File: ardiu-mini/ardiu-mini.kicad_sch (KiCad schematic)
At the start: 6 parts

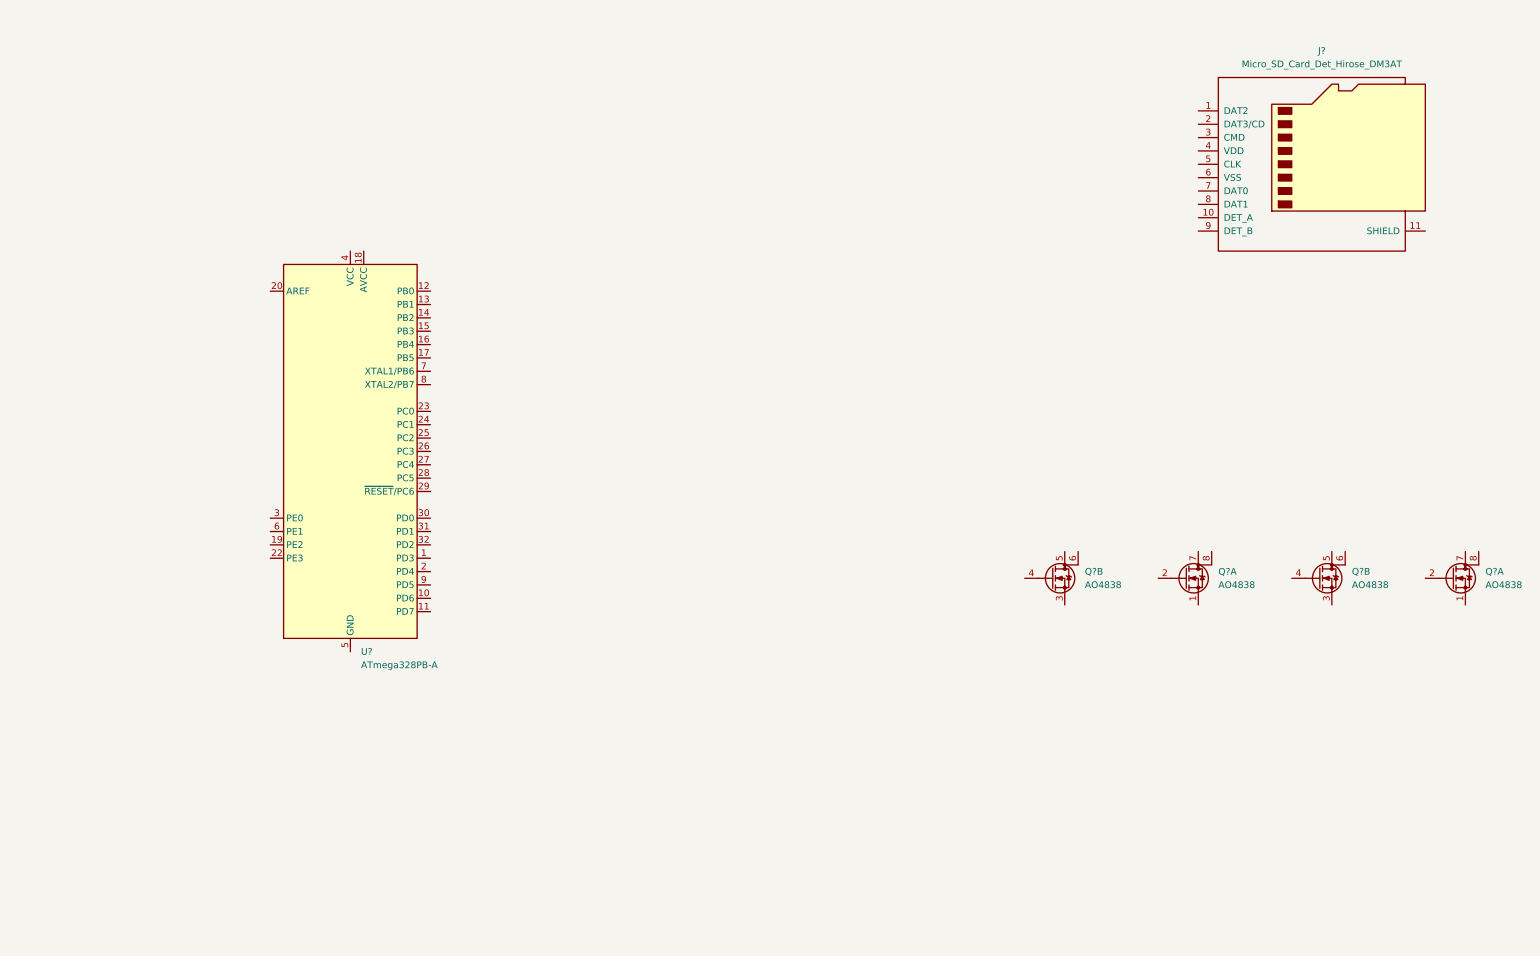
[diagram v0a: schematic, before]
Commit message: Board layout with weak grounding path
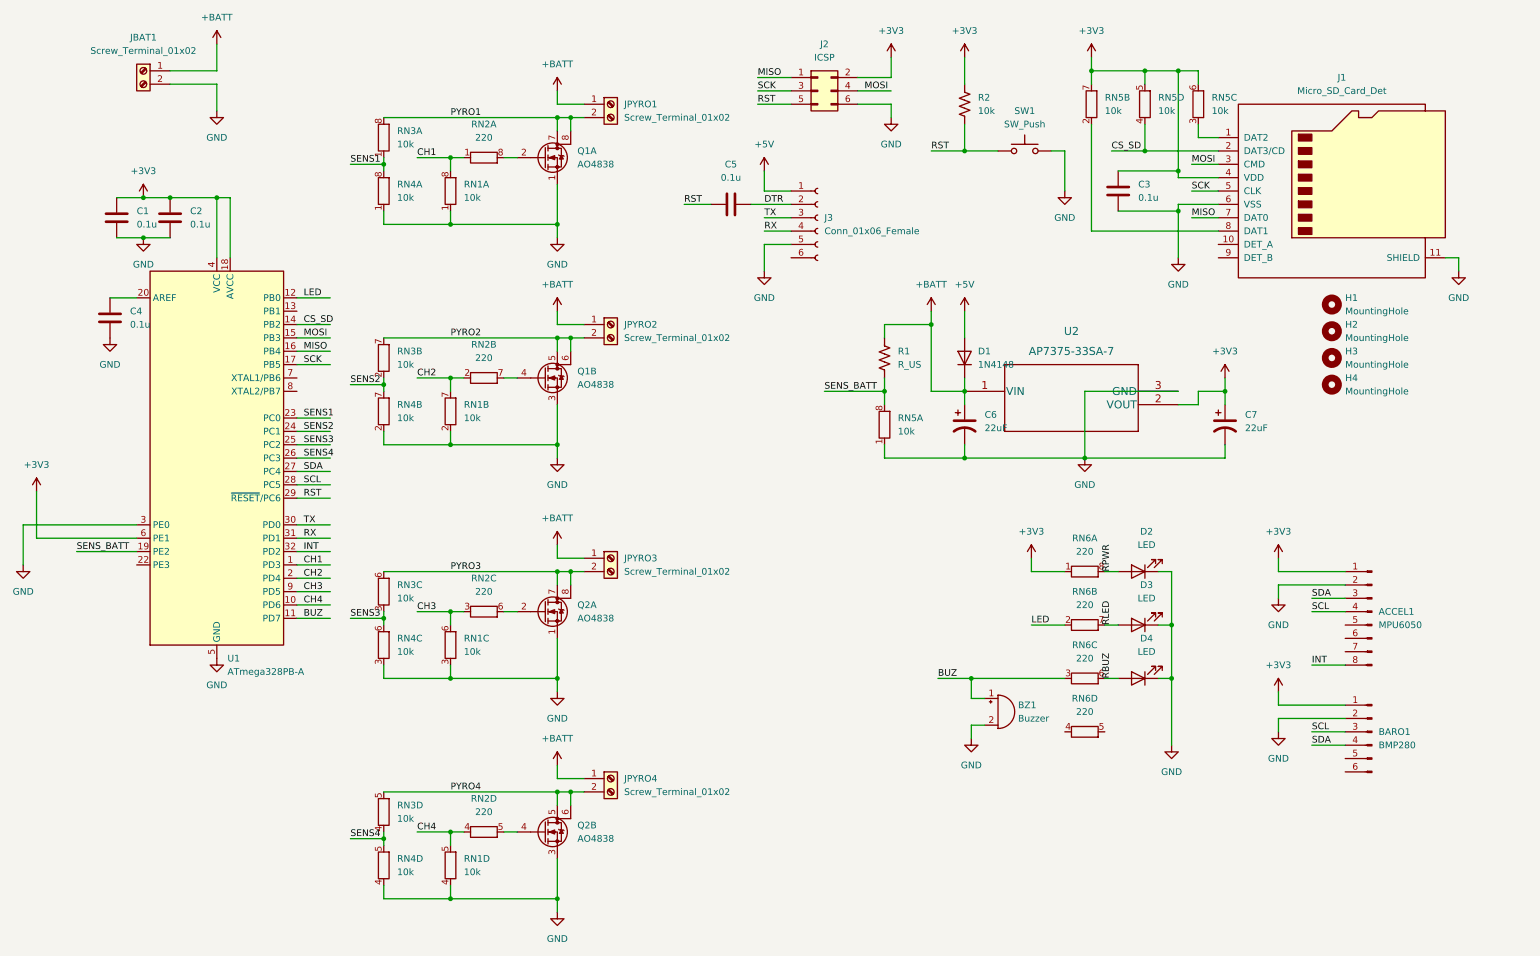
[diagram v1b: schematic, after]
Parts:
- removed J?: Micro_SD_Card_Det_Hirose_DM3AT, Connector_Card:microSD_HC_Molex_104031-0811, symbol Connector:Micro_SD_Card_Det_Hirose_DM3AT
- added ACCEL1: MPU6050, Sensor_BreakoutBoards:Breakout_MPU6050_Generic, symbol Connector:Conn_01x08_Male
- added BARO1: BMP280, Sensor_BreakoutBoards:Breakout_BMP280_Generic, symbol Connector:Conn_01x06_Male
- added BZ1: Buzzer, Buzzer_Beeper:Buzzer_12x9.5RM7.6, symbol Device:Buzzer
- added C1, C2, C4, C5: 0.1u, Capacitor_SMD:C_0805_2012Metric_Pad1.18x1.45mm_HandSolder, symbol Device:C
- added C3: 0.1u, symbol Device:C
- added C6, C7: 22uF, Capacitor_SMD:C_1206_3216Metric_Pad1.33x1.80mm_HandSolder, symbol Device:C_Polarized_US
- added D1: 1N4148, Diode_THT:D_DO-35_SOD27_P7.62mm_Horizontal, symbol Diode:1N4148
- added D2: LED, symbol Device:LED
- added D3, D4: LED, LED_THT:LED_D3.0mm, symbol Device:LED
- added H1, H2, H3: MountingHole, MountingHole:MountingHole_3.2mm_M3, symbol Mechanical:MountingHole
- added H4: MountingHole, symbol Mechanical:MountingHole
- added J1: Micro_SD_Card_Det, Connector_Amphenol_Custom:Connector_Amphenol_MicroSD_PushPull, symbol Connector:Micro_SD_Card_Det
- added J2: ICSP, Connector_PinHeader_2.54mm:PinHeader_2x03_P2.54mm_Vertical, symbol Connector_Generic:Conn_02x03_Odd_Even
- added J3: Conn_01x06_Female, symbol Connector:Conn_01x06_Female
- added JBAT1, JPYRO1, JPYRO2, JPYRO3, JPYRO4: Screw_Terminal_01x02, TerminalBlock_TE-Connectivity:TerminalBlock_TE_282834-2_1x02_P2.54mm_Horizontal, symbol Connector:Screw_Terminal_01x02
- added R1: R_US, Resistor_SMD:R_0805_2012Metric_Pad1.20x1.40mm_HandSolder, symbol Device:R_US
- added R2: 10k, Resistor_SMD:R_0805_2012Metric_Pad1.20x1.40mm_HandSolder, symbol Device:R_US
- added RN1, RN3, RN4, RN5: 10k, Resistor_SMD:R_Array_Concave_4x0603, symbol Device:R_Pack04_Split
- added RN2: 220, symbol Device:R_Pack04_Split
- added RN6: 220, Resistor_SMD:R_Array_Concave_4x0603, symbol Device:R_Pack04_Split
- added SW1: SW_Push, Button_Switch_THT:SW_PUSH_6mm, symbol Switch:SW_Push
- added U2: AP7375-33SA-7, Package_TO_SOT_SMD:SOT-23_Handsoldering, symbol Regulator_Linear_Custom:AP7375-33SA-7
- Q1: renamed from Q?; footprint (none) -> Package_SO:SO-8_3.9x4.9mm_P1.27mm
- gave numbers to parts that had none: 2
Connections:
- net GND: now reaches Q2.1 (S)
- net GND: now also Q1.1 (S), Q1.3 (S), Q2.3 (S), U1.21 (GND), U1.3 (PE0), U1.5 (GND), ACCEL1.2 (Pin_2), BARO1.2 (Pin_2), BZ1.2 (+), C1.2, C2.2, C3.2, C4.2, C6.2, C7.2, D2.1 (K), D3.1 (K), D4.1 (K), J1.11 (SHIELD), J1.6 (VSS), J2.6 (Pin_6), J3.5 (Pin_5), JBAT1.2 (Pin_2), RN1.1 (R1.1), RN1.2 (R2.1), RN1.3 (R3.1), RN1.4 (R4.1), RN4.1 (R1.1), RN4.2 (R2.1), RN4.3 (R3.1), RN4.4 (R4.1), RN5.1 (R1.1), SW1.2, U2.3 (GND)
- net at Q2.2 (G): now also RN2.6 (R3.2)
- net PYRO3: now reaches Q2.7 (D)
- net PYRO3: now also Q2.8 (D), JPYRO3.2 (Pin_2), RN3.6 (R3.2)
- net CH1: now reaches U1.1 (PD3)
- net CH1: now also RN1.8 (R1.2), RN2.1 (R1.1)
- net CH4: now reaches U1.10 (PD6)
- net CH4: now also RN1.5 (R4.2), RN2.4 (R4.1)
- net BUZ: now reaches U1.11 (PD7)
- net BUZ: now also BZ1.1 (-), RN6.3 (R3.1)
- net LED: now reaches U1.12 (PB0)
- net LED: now also RN6.2 (R2.1)
- net CS_SD: now reaches U1.14 (PB2)
- net CS_SD: now also J1.2 (DAT3/CD), RN5.4 (R4.1)
- net MOSI: now reaches U1.15 (PB3)
- net MOSI: now also J1.3 (CMD), J2.4 (Pin_4)
- net MISO: now reaches U1.16 (PB4)
- net MISO: now also J1.7 (DAT0), J2.1 (Pin_1)
- net SCK: now reaches U1.17 (PB5)
- net SCK: now also J1.5 (CLK), J2.3 (Pin_3)
- net +3V3: now reaches U1.18 (AVCC)
- net +3V3: now also U1.4 (VCC), U1.6 (PE1), ACCEL1.1 (Pin_1), BARO1.1 (Pin_1), C1.1, C2.1, C3.1, C7.1, J1.4 (VDD), J2.2 (Pin_2), R2.1, RN5.5 (R4.2), RN5.6 (R3.2), RN5.7 (R2.2), RN6.1 (R1.1), U2.2 (VOUT)
- net SENS_BATT: now reaches U1.19 (PE2)
- net SENS_BATT: now also R1.2, RN5.8 (R1.2)
- net CH2: now reaches U1.2 (PD4)
- net CH2: now also RN1.7 (R2.2), RN2.2 (R2.1)
- net at U1.20 (AREF): now also C4.1
- net SENS1: now reaches U1.23 (PC0)
- net SENS1: now also RN3.1 (R1.1), RN4.8 (R1.2)
- net SENS2: now reaches U1.24 (PC1)
- net SENS2: now also RN3.2 (R2.1), RN4.7 (R2.2)
- net SENS3: now reaches U1.25 (PC2)
- net SENS3: now also RN3.3 (R3.1), RN4.6 (R3.2)
- net SENS4: now reaches U1.26 (PC3)
- net SENS4: now also RN3.4 (R4.1), RN4.5 (R4.2)
- net SDA: now reaches U1.27 (PC4)
- net SDA: now also ACCEL1.3 (Pin_3), BARO1.4 (Pin_4)
- net SCL: now reaches U1.28 (PC5)
- net SCL: now also ACCEL1.4 (Pin_4), BARO1.3 (Pin_3)
- net RST: now reaches U1.29 (~{RESET}/PC6)
- net RST: now also C5.1, J2.5 (Pin_5), R2.2, SW1.1
- net TX: now reaches U1.30 (PD0)
- net TX: now also J3.3 (Pin_3)
- net RX: now reaches U1.31 (PD1)
- net RX: now also J3.4 (Pin_4)
- net INT: now reaches U1.32 (PD2)
- net INT: now also ACCEL1.8 (Pin_8)
- net CH3: now reaches U1.9 (PD5)
- net CH3: now also RN1.6 (R3.2), RN2.3 (R3.1)
- net at Q1.4 (G): now also RN2.7 (R2.2)
- net PYRO2: now reaches Q1.5 (D)
- net PYRO2: now also Q1.6 (D), JPYRO2.2 (Pin_2), RN3.7 (R2.2)
- net at Q2.4 (G): now also RN2.5 (R4.2)
- net PYRO4: now reaches Q2.5 (D)
- net PYRO4: now also Q2.6 (D), JPYRO4.2 (Pin_2), RN3.5 (R4.2)
- net at Q1.2 (G): now also RN2.8 (R1.2)
- net PYRO1: now reaches Q1.7 (D)
- net PYRO1: now also Q1.8 (D), JPYRO1.2 (Pin_2), RN3.8 (R1.2)
- new net: J1.1 (DAT2), RN5.3 (R3.1)
- new net: J1.8 (DAT1), RN5.2 (R2.1)
- new net +5V: D1.2 (A), J3.1 (Pin_1)
- new net +BATT: C6.1, D1.1 (K), JBAT1.1 (Pin_1), JPYRO1.1 (Pin_1), JPYRO2.1 (Pin_1), JPYRO3.1 (Pin_1), JPYRO4.1 (Pin_1), R1.1, U2.1 (VIN)
- new net DTR: C5.2, J3.2 (Pin_2)
- new net RBUZ: D4.2 (A), RN6.6 (R3.2)
- new net RLED: D3.2 (A), RN6.7 (R2.2)
- new net RPWR: D2.2 (A), RN6.8 (R1.2)
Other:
- moved on the sheet: Q1A, Q1B, Q2A, Q2B, U1

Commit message: Fixed some errors, added actually 5V safe debug ports
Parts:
- added RN7: 2200, Resistor_SMD:R_Array_Concave_4x0603, symbol Device:R_Pack04_Split
- added TPX1, TPX2: x, TestPoint:TestPoint_Pad_D1.5mm, symbol Connector:TestPoint
- C3: footprint (none) -> Capacitor_SMD:C_0805_2012Metric_Pad1.18x1.45mm_HandSolder
- D2: footprint (none) -> LED_THT:LED_D3.0mm
- H4: footprint (none) -> MountingHole:MountingHole_3.2mm_M3
- J3: footprint (none) -> Connector_PinSocket_2.54mm:PinSocket_1x06_P2.54mm_Vertical
- R1: value R_US -> 100k
- RN2: footprint (none) -> Resistor_SMD:R_Array_Concave_4x0603
- RN3: value 10k -> 100k
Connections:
- net +3V3: no longer J2.2 (Pin_2)
- net +5V: now also J2.2 (Pin_2)
- net DTR: now also C5.1, J3.5 (Pin_5); no longer C5.2, J3.2 (Pin_2)
- net GND: now also J3.2 (Pin_2); no longer J3.5 (Pin_5)
- net MOSI: now also RN7.2 (R2.1); no longer J2.4 (Pin_4)
- net PYRO1: now also RN3.5 (R4.2); no longer RN3.8 (R1.2)
- net PYRO2: now also RN3.6 (R3.2); no longer RN3.7 (R2.2)
- net PYRO3: now also RN3.7 (R2.2); no longer RN3.6 (R3.2)
- net PYRO4: now also RN3.8 (R1.2); no longer RN3.5 (R4.2)
- net RST: now also C5.2; no longer C5.1
- net RX: now also RN7.1 (R1.1); no longer J3.4 (Pin_4)
- net SCK: now also RN7.3 (R3.1); no longer J2.3 (Pin_3)
- net SCL: now also ACCEL1.3 (Pin_3); no longer ACCEL1.4 (Pin_4)
- net SDA: now also ACCEL1.4 (Pin_4); no longer ACCEL1.3 (Pin_3)
- net SENS1: now also RN3.4 (R4.1), RN4.5 (R4.2); no longer RN3.1 (R1.1), RN4.8 (R1.2)
- net SENS2: now also RN3.3 (R3.1), RN4.6 (R3.2); no longer RN3.2 (R2.1), RN4.7 (R2.2)
- net SENS3: now also RN3.2 (R2.1), RN4.7 (R2.2); no longer RN3.3 (R3.1), RN4.6 (R3.2)
- net SENS4: now also RN3.1 (R1.1), RN4.8 (R1.2); no longer RN3.4 (R4.1), RN4.5 (R4.2)
- net XTAL1: now reaches U1.7 (XTAL1/PB6)
- net XTAL1: now also TPX1.1
- net XTAL2: now reaches U1.8 (XTAL2/PB7)
- net XTAL2: now also TPX2.1
- new net 5MOSI: J2.4 (Pin_4), RN7.7 (R2.2)
- new net 5RX: J3.4 (Pin_4), RN7.8 (R1.2)
- new net 5SCK: J2.3 (Pin_3), RN7.6 (R3.2)
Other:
- note added: "Arduino Pin Assignments 0: RX 1: TX 2: Gyro Interrupt 3: Channel 1 Out 4: Channel 2 Out 5: Channel 3 Out 6: Channel 4 Out 7: Buzzer 8: LED 9: 10: SPI CS SD 11: SPI MOSI 12: SPI MISO 13: SPI SCK A0: Channel 1 sense A1: Channel 2 sense A2: Channel 3 sense A3: Channel 4 sense A4: SDA A5: SCL A6: Battery sense A7:"
- moved on the sheet: C5, J2, JPYRO1, JPYRO2, JPYRO3, JPYRO4, Q1A, Q1B, Q2A, Q2B, RN1A, RN1B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
